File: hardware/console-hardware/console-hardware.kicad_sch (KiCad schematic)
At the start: 52 parts, among them J1 USB_B_Micro, J2 LiPo battery, J3 Conn_01x04, J4 ICSP, J5 Conn_01x20, SW1 SW_Push, SW2 SW_Push, SW3 SW_Push, SW4 SW_Push, SW5 SW_Push, SW6 SW_Push, SW7 SW_SPDT, U1 ATmega32U4-A, U2 MCP73831-2-OT, U3 MIC5219-3.3YM5, X1 16 MHz

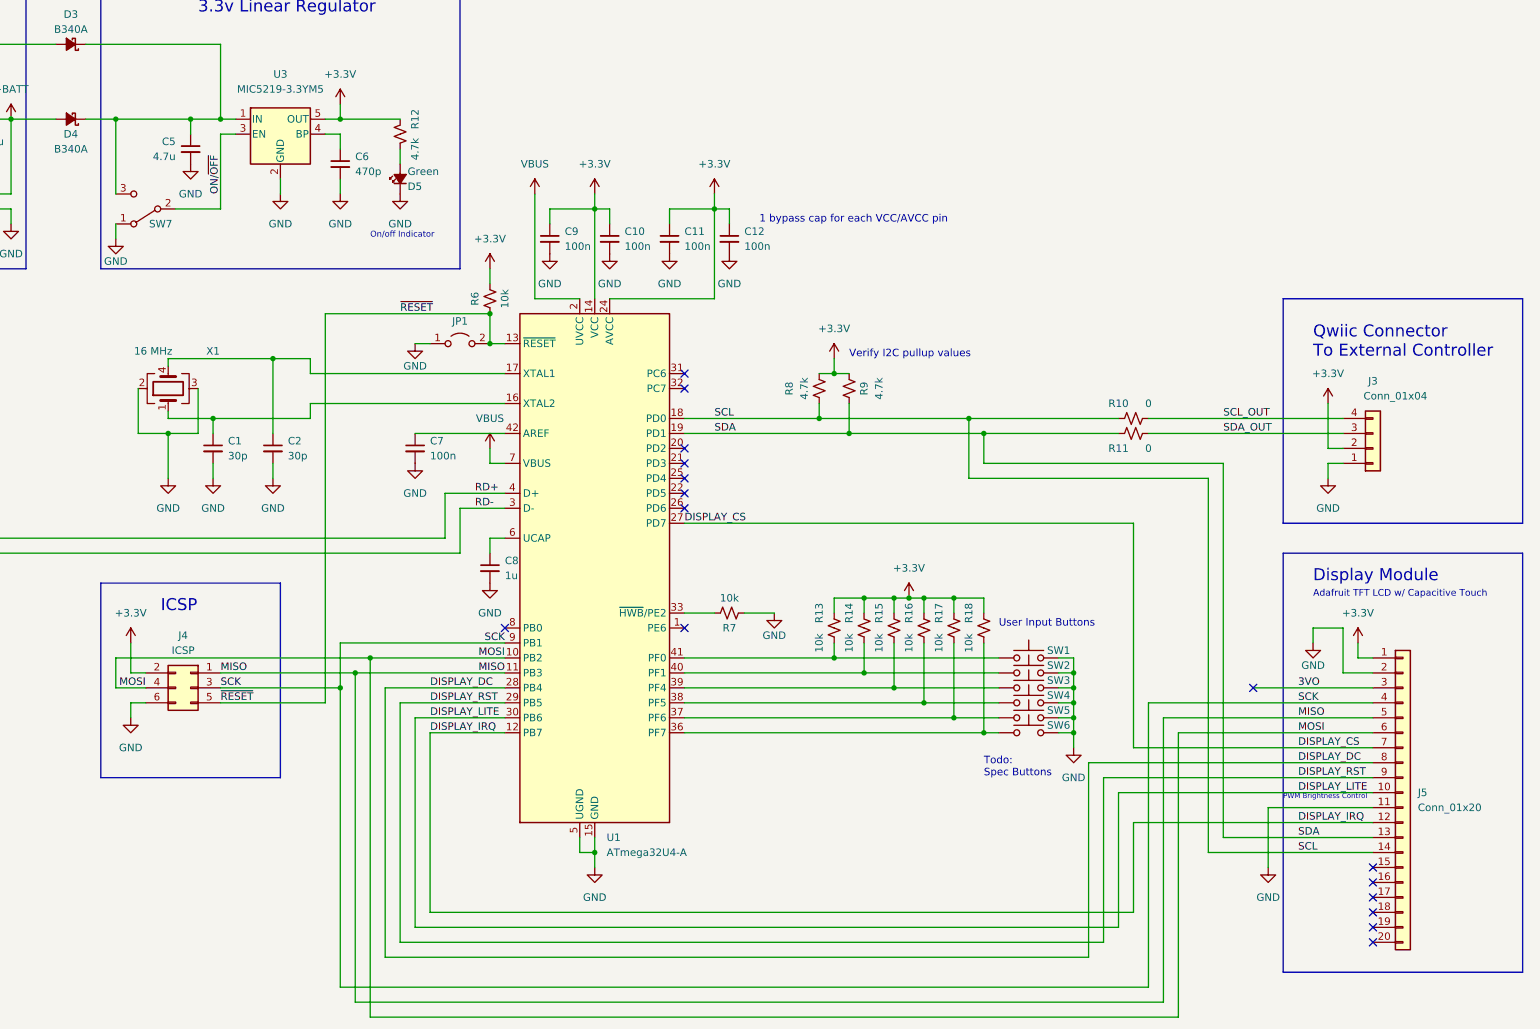
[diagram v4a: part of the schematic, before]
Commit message: Updated board layout, some small schematic fixes, and added 3D models
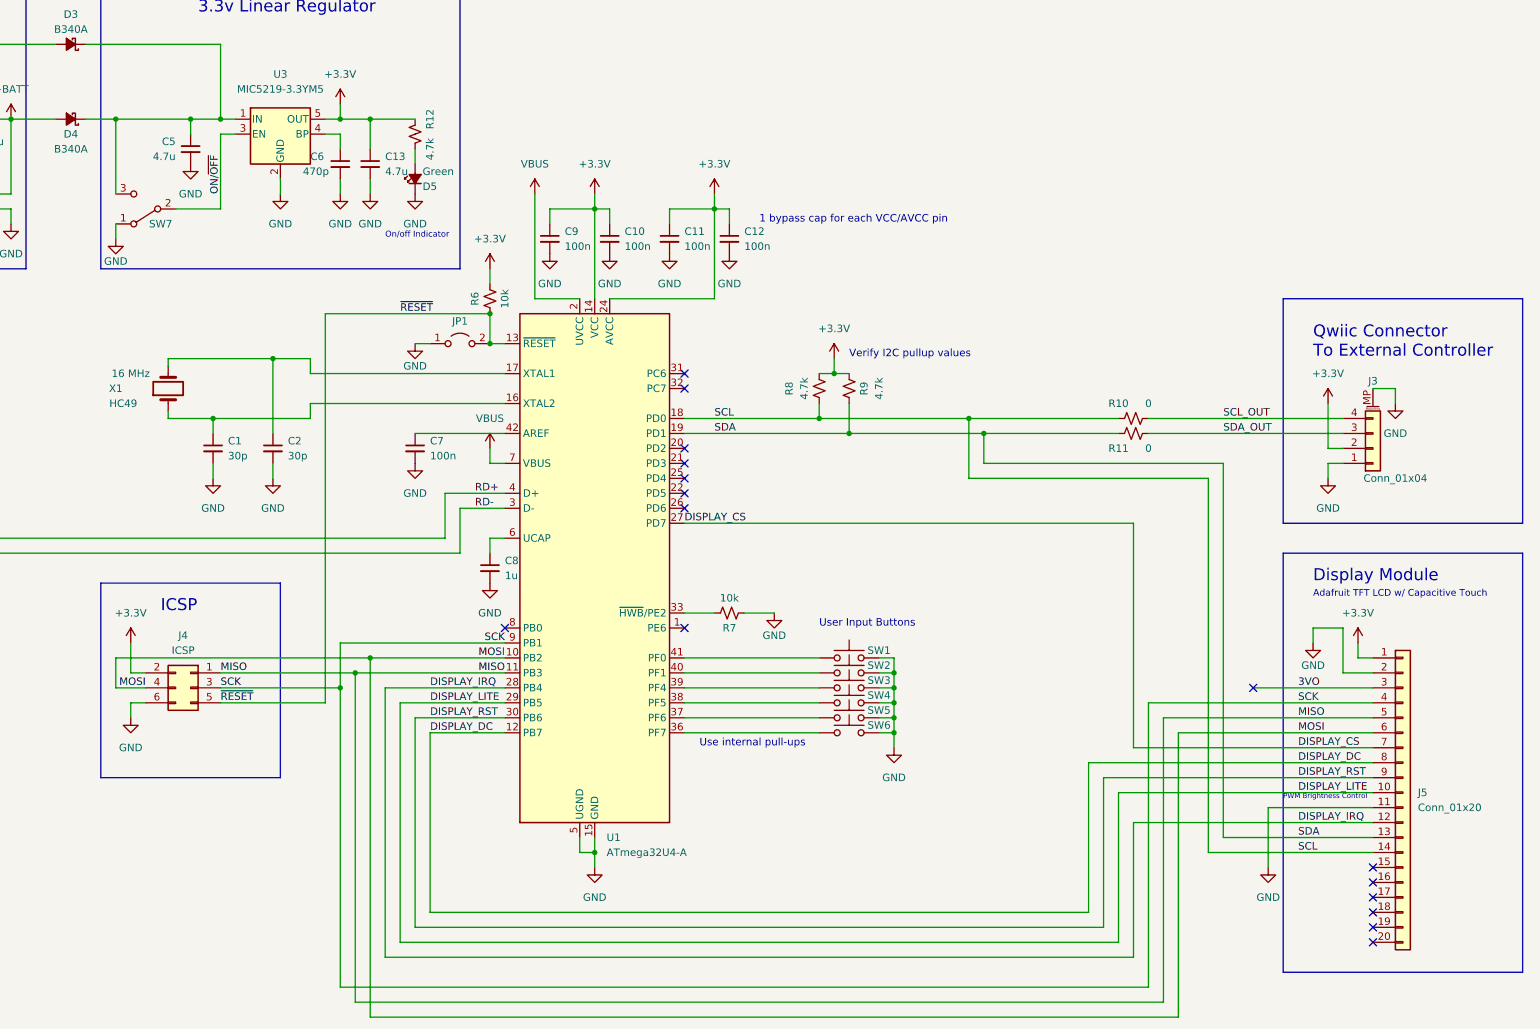
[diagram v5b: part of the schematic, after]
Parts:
- removed R13, R14, R15, R16, R17, R18: 10k, Resistor_SMD:R_0805_2012Metric, symbol Device:R_Small_US
- added C13: 4.7u, Capacitor_SMD:C_0805_2012Metric, symbol Device:C_Small
- J1: footprint Connector_USB:USB_Micro-B_Amphenol_10104110_Horizontal -> USB-Conn:WE_629105136821
- J3: symbol Connector_Generic:Conn_01x04 -> Connector_Generic_MountingPin:Conn_01x04_MountingPin
- SW1, SW2, SW3, SW4, SW5, SW6: footprint Button_Switch_SMD:SW_SPST_TL3305A -> Button_Switch_THT:SW_TH_Tactile_Omron_B3F-10xx
- SW7: footprint Button_Switch_THT:SW_E-Switch_EG1224_SPDT_Angled -> SW-EG1213:SW_EG1213
- X1: footprint Crystal:Crystal_SMD_2520-4Pin_2.5x2.0mm -> Crystal:Crystal_SMD_HC49-SD; symbol Device:Crystal_GND23 -> Device:Crystal; Field8 (none) -> HC49
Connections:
- net +3.3V: now also C13.1
- net DISPLAY_DC: now also U1.12 (PB7); no longer U1.28 (PB4)
- net DISPLAY_IRQ: now also U1.28 (PB4); no longer U1.12 (PB7)
- net DISPLAY_LITE: now also U1.29 (PB5); no longer U1.30 (PB6)
- net DISPLAY_RST: now also U1.30 (PB6); no longer U1.29 (PB5)
- net GND: now also J3.MP (MountPin), C13.2; no longer X1.2, X1.3
- net at C2.1, U1.17 (XTAL1): now also X1.2; no longer X1.4
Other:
- note added: "Use internal pull-ups"
- note removed: "Todo: Spec Buttons"
- moved on the sheet: D5, R12, SW1, SW2, SW3, SW4, SW5, SW6

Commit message: Updated board, fixed drc errors, added mounting holes and test points, added name
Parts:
- added TP1, TP10, TP11, TP12, TP13, TP14, TP15, TP16, TP2, TP3, TP4, TP5, TP6, TP7, TP8, TP9: Test-Point, Testpoints:1X01, symbol TestPoint:Test-Point
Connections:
- net +3.3V: now also J5.2 (Pin_2), TP6.1; no longer J5.1 (Pin_1)
- net +BATT: now also TP3.1
- net DISPLAY_CS: now also TP11.1
- net DISPLAY_DC: now also TP9.1
- net DISPLAY_IRQ: now also TP13.1
- net DISPLAY_LITE: now also TP12.1
- net DISPLAY_RST: now also TP10.1
- net GND: now also J5.1 (Pin_1), TP1.1; no longer J5.2 (Pin_2)
- net ON/~{OFF}: now also TP5.1
- net SCL: now also TP7.1
- net SDA: now also TP8.1
- net VBUS: now also TP2.1
- net at C5.1, D3.1 (K), D4.1 (K)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: now also TP4.1
- net at U1.20 (PD2): now also TP14.1
- net at U1.21 (PD3): now also TP15.1
- net at U1.22 (PD5): now also TP16.1
- no-connect marks 17 -> 14

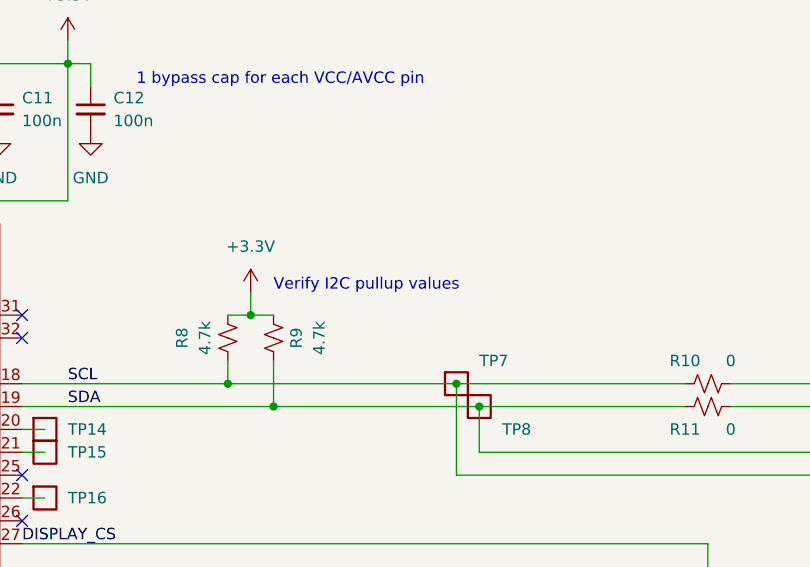
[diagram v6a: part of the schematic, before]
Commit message: Finishing touches to the PCB. Updated attributes for parts.
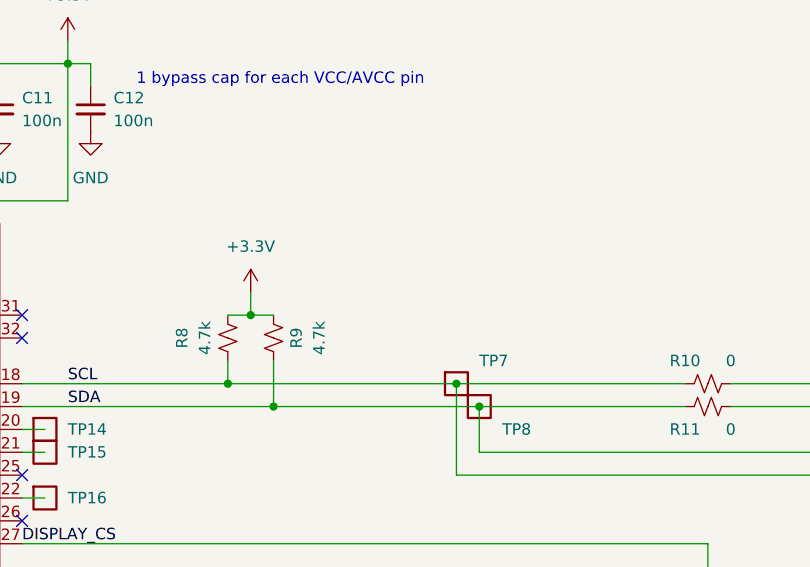
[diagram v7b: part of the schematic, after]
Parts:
- J1: DPN WM1398CT-ND -> 732-3155-1-ND; MFR Molex -> Wurth; MPN 0476420001 -> 629105136821
- SW1, SW2, SW3, SW4, SW5, SW6: DIS Adafruit -> Digi-Key; DPN 1010 -> SW405-ND; MFR (none) -> Omron; MPN (none) -> B3F-1052
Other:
- note removed: "Verify I2C pullup values"
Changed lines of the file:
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@@
     (effects (font (size 2.032 2.032)) (justify left bottom))
-  )
-  (text "Verify I2C pullup values" (at 279.4 114.3 0)
-    (effects (font (size 1.27 1.27)) (justify left bottom))
   )
   (text "Qwiic Connector\nTo External Controller" (at 358.14 114.3 0)
@@
       (effects (font (size 1.27 1.27)) hide)
     )
-    (property "DIS" "Adafruit" (id 4) (at 279.4 175.26 0)
-      (effects (font (size 1.27 1.27)) hide)
-    )
-    (property "DPN" "1010" (id 5) (at 279.4 175.26 0)
+    (property "DIS" "Digi-Key" (id 4) (at 279.4 175.26 0)
+      (effects (font (size 1.27 1.27)) hide)
+    )
+    (property "DPN" "SW405-ND" (id 5) (at 279.4 175.26 0)
+      (effects (font (size 1.27 1.27)) hide)
+    )
+    (property "MFR" "Omron" (id 6) (at 279.4 175.26 0)
+      (effects (font (size 1.27 1.27)) hide)
+    )
+    (property "MPN" "B3F-1052" (id 7) (at 279.4 175.26 0)
       (effects (font (size 1.27 1.27)) hide)
     )
@@
       (effects (font (size 1.27 1.27)) hide)
     )
-    (property "DIS" "Adafruit" (id 4) (at 279.4 170.18 0)
-      (effects (font (size 1.27 1.27)) hide)
-    )
-    (property "DPN" "1010" (id 5) (at 279.4 170.18 0)
+    (property "DIS" "Digi-Key" (id 4) (at 279.4 170.18 0)
+      (effects (font (size 1.27 1.27)) hide)
+    )
+    (property "DPN" "SW405-ND" (id 5) (at 279.4 170.18 0)
+      (effects (font (size 1.27 1.27)) hide)
+    )
+    (property "MFR" "Omron" (id 6) (at 279.4 170.18 0)
+      (effects (font (size 1.27 1.27)) hide)
+    )
+    (property "MPN" "B3F-1052" (id 7) (at 279.4 170.18 0)
       (effects (font (size 1.27 1.27)) hide)
     )
@@
       (effects (font (size 1.27 1.27)) hide)
     )
-    (property "DIS" "Adafruit" (id 4) (at 279.4 172.72 0)
-      (effects (font (size 1.27 1.27)) hide)
-    )
-    (property "DPN" "1010" (id 5) (at 279.4 172.72 0)
+    (property "DIS" "Digi-Key" (id 4) (at 279.4 172.72 0)
+      (effects (font (size 1.27 1.27)) hide)
+    )
+    (property "DPN" "SW405-ND" (id 5) (at 279.4 172.72 0)
+      (effects (font (size 1.27 1.27)) hide)
+    )
+    (property "MFR" "Omron" (id 6) (at 279.4 172.72 0)
+      (effects (font (size 1.27 1.27)) hide)
+    )
+    (property "MPN" "B3F-1052" (id 7) (at 279.4 172.72 0)
       (effects (font (size 1.27 1.27)) hide)
     )
@@
       (effects (font (size 1.27 1.27)) hide)
     )
-    (property "DIS" "Adafruit" (id 4) (at 279.4 167.64 0)
-      (effects (font (size 1.27 1.27)) hide)
-    )
-    (property "DPN" "1010" (id 5) (at 279.4 167.64 0)
+    (property "DIS" "Digi-Key" (id 4) (at 279.4 167.64 0)
+      (effects (font (size 1.27 1.27)) hide)
+    )
+    (property "DPN" "SW405-ND" (id 5) (at 279.4 167.64 0)
+      (effects (font (size 1.27 1.27)) hide)
+    )
+    (property "MFR" "Omron" (id 6) (at 279.4 167.64 0)
+      (effects (font (size 1.27 1.27)) hide)
+    )
+    (property "MPN" "B3F-1052" (id 7) (at 279.4 167.64 0)
       (effects (font (size 1.27 1.27)) hide)
     )
@@
       (effects (font (size 1.27 1.27)) hide)
     )
-    (property "DIS" "Adafruit" (id 4) (at 279.4 165.1 0)
-      (effects (font (size 1.27 1.27)) hide)
-    )
-    (property "DPN" "1010" (id 5) (at 279.4 165.1 0)
+    (property "DIS" "Digi-Key" (id 4) (at 279.4 165.1 0)
+      (effects (font (size 1.27 1.27)) hide)
+    )
+    (property "DPN" "SW405-ND" (id 5) (at 279.4 165.1 0)
+      (effects (font (size 1.27 1.27)) hide)
+    )
+    (property "MFR" "Omron" (id 6) (at 279.4 165.1 0)
+      (effects (font (size 1.27 1.27)) hide)
+    )
+    (property "MPN" "B3F-1052" (id 7) (at 279.4 165.1 0)
       (effects (font (size 1.27 1.27)) hide)
     )
@@
       (effects (font (size 1.27 1.27)) hide)
     )
-    (property "DIS" "Adafruit" (id 4) (at 279.4 177.8 0)
-      (effects (font (size 1.27 1.27)) hide)
-    )
-    (property "DPN" "1010" (id 5) (at 279.4 177.8 0)
+    (property "DIS" "Digi-Key" (id 4) (at 279.4 177.8 0)
+      (effects (font (size 1.27 1.27)) hide)
+    )
+    (property "DPN" "SW405-ND" (id 5) (at 279.4 177.8 0)
+      (effects (font (size 1.27 1.27)) hide)
+    )
+    (property "MFR" "Omron" (id 6) (at 279.4 177.8 0)
+      (effects (font (size 1.27 1.27)) hide)
+    )
+    (property "MPN" "B3F-1052" (id 7) (at 279.4 177.8 0)
       (effects (font (size 1.27 1.27)) hide)
     )
@@
       (effects (font (size 1.27 1.27)) hide)
     )
-    (property "DPN" "WM1398CT-ND" (id 5) (at 55.88 132.08 0)
-      (effects (font (size 1.27 1.27)) hide)
-    )
-    (property "MFR" "Molex" (id 6) (at 55.88 132.08 0)
-      (effects (font (size 1.27 1.27)) hide)
-    )
-    (property "MPN" "0476420001" (id 7) (at 55.88 132.08 0)
-      (effects (font (size 1.27 1.27)) hide)
-    )
+    (property "DPN" "732-3155-1-ND" (id 5) (at 55.88 132.08 0)
+      (effects (font (size 1.27 1.27)) hide)
+    )
+    (property "MFR" "Wurth" (id 6) (at 55.88 132.08 0)
+      (effects (font (size 1.27 1.27)) hide)
+    )
+    (property "MPN" "629105136821" (id 7) (at 55.88 132.08 0)
+      (effects (font (size 1.27 1.27)) hide)
+    )
